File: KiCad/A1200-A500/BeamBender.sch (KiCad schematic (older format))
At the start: 30 parts, among them J1 4-1734742-0, J2 HDMI_A_1.4, J3 STX-3501-3N, J4 Phoenix_Contact, U1 LM1117-3.3, U3 ADV7513BSWZ, X1 Abracon ASE-27.000MHZ-L-R-T

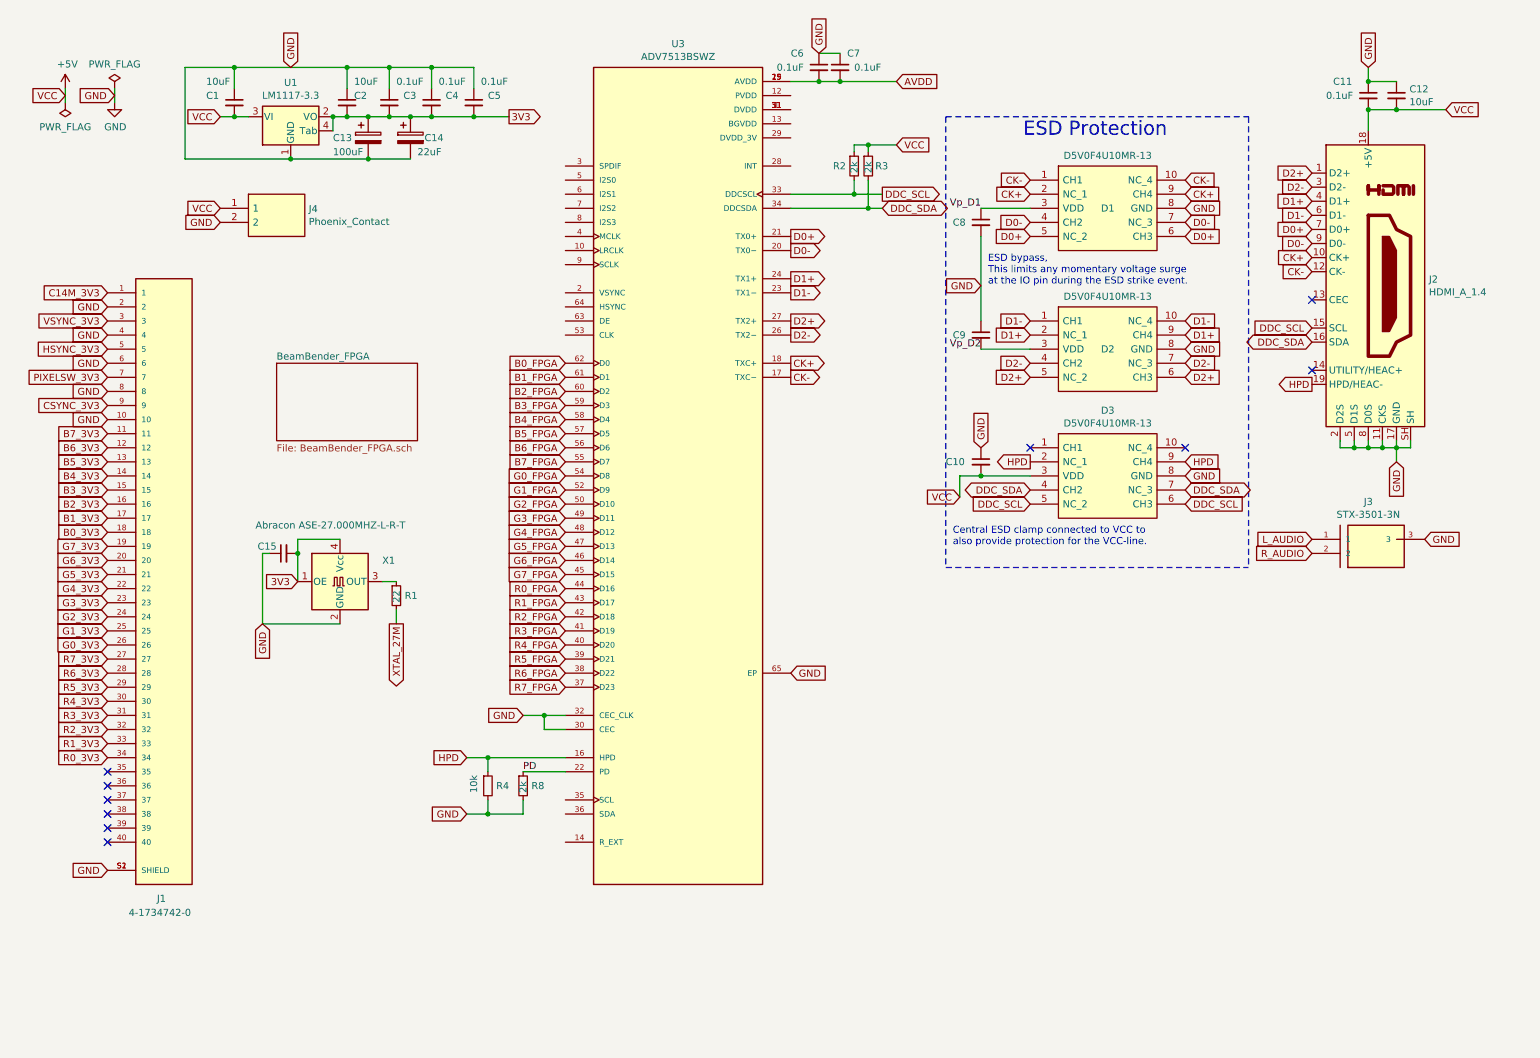
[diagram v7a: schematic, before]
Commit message: Changed to four layer stackup, added some caps and done some more routing
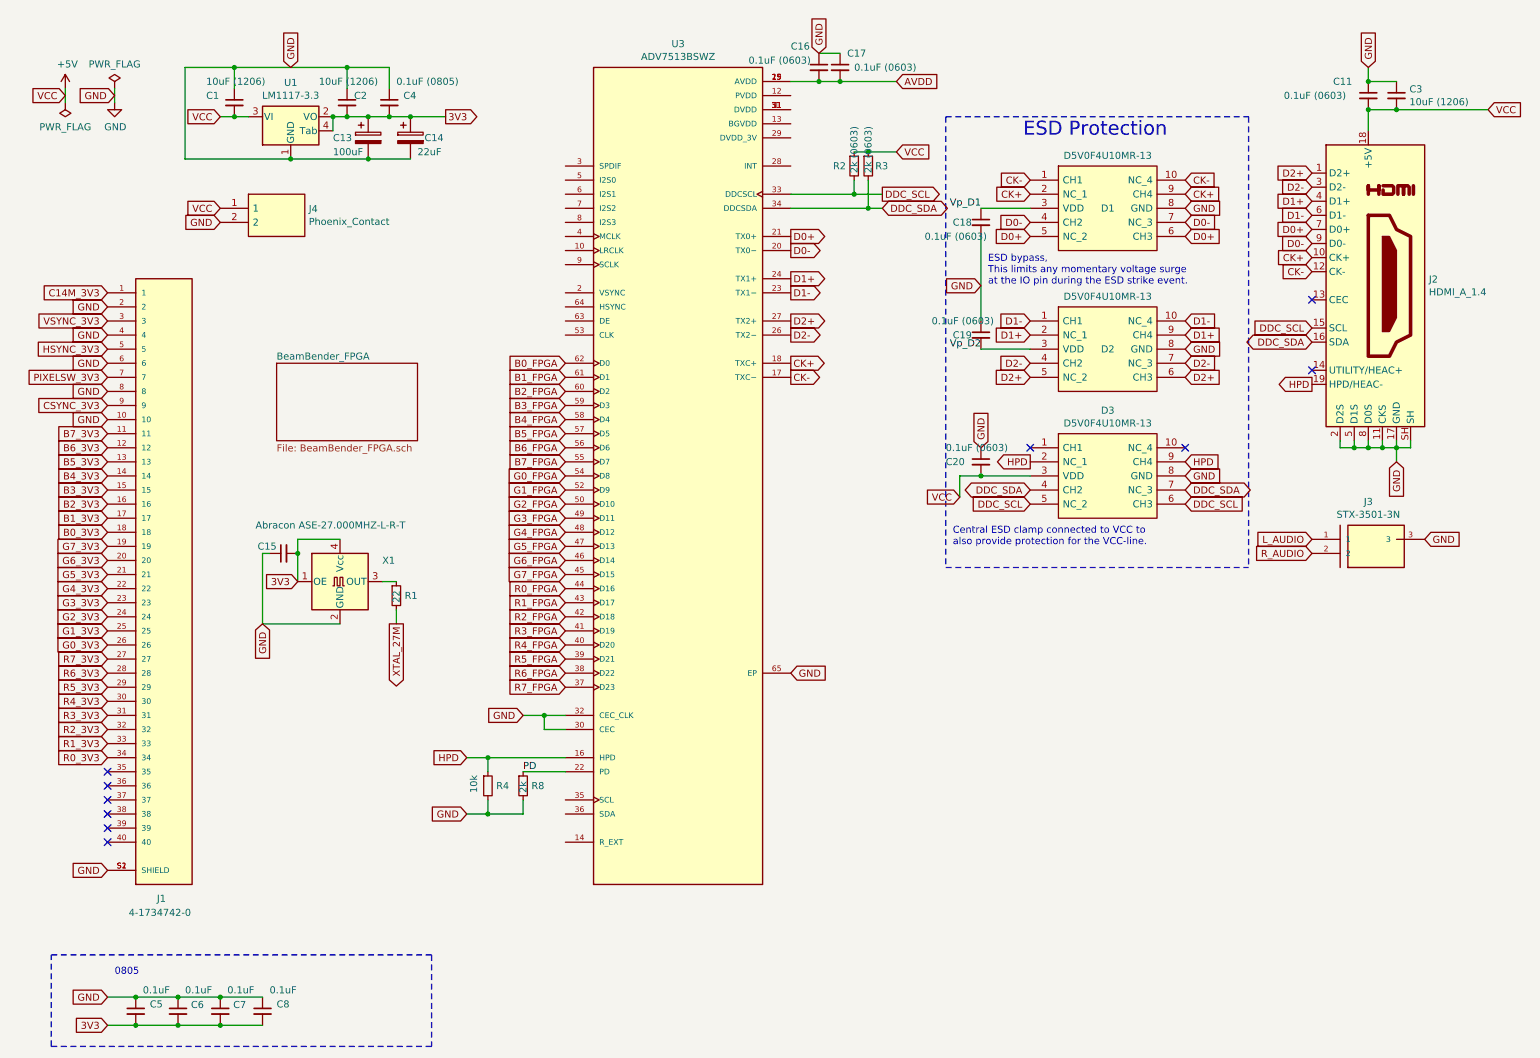
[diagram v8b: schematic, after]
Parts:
- added C6, C7: 0.1uF, Capacitor_SMD:C_0805_2012Metric_Pad1.18x1.45mm_HandSolder, symbol Device:C_Small
- C1, C2: value 10uF -> 10uF (1206)
- C11: value 0.1uF -> 0.1uF (0603)
- C16: renamed from C6; value 0.1uF -> 0.1uF (0603)
- C17: renamed from C7; value 0.1uF -> 0.1uF (0603)
- C18: renamed from C8; value 0.1uF -> 0.1uF (0603)
- C19: renamed from C9; value 0.1uF -> 0.1uF (0603)
- C20: renamed from C10; value 0.1uF -> 0.1uF (0603)
- C3: renamed from C12; value 10uF -> 10uF (1206)
- C4: renamed from C3; value 0.1uF -> 0.1uF (0805)
- R2, R3: value 2k -> 2k (0603)
- renumbered C4 to C5, C5 to C8
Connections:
- net 3V3: now also C6.2, C7.2
- net GND: now also C6.1, C7.1
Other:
- note added: "0805"
- moved on the sheet: C5, C8
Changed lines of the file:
@@
 Text GLabel 2450 800  1    50   Input ~ 0
 GND
-Text GLabel 4000 1150 2    50   Output ~ 0
+Text GLabel 3550 1150 2    50   Output ~ 0
 3V3
 $Comp
@@
 P 2050 1050
 F 0 "C1" H 1850 1100 50  0000 L CNN
-F 1 "10uF" H 1850 1200 50  0000 L CNN
+F 1 "10uF (1206)" H 1850 1200 50  0000 L CNN
 F 2 "Capacitor_SMD:C_1206_3216Metric_Pad1.42x1.75mm_HandSolder" H 2050 1050 50  0001 C CNN
 F 3 "~" H 2050 1050 50  0001 C CNN
@@
 $EndComp
 $Comp
-L Device:C_Small C3
+L Device:C_Small C4
 U 1 1 62475F7C
 P 3150 1050
-F 0 "C3" H 3250 1100 50  0000 L CNN
-F 1 "0.1uF" H 3200 1200 50  0000 L CNN
+F 0 "C4" H 3250 1100 50  0000 L CNN
+F 1 "0.1uF (0805)" H 3200 1200 50  0000 L CNN
 F 2 "Capacitor_SMD:C_0805_2012Metric_Pad1.15x1.40mm_HandSolder" H 3150 1050 50  0001 C CNN
 F 3 "~" H 3150 1050 50  0001 C CNN
@@
 	3150 950  3150 800
 $Comp
-L Device:C_Small C4
+L Device:C_Small C5
 U 1 1 624DDB45
-P 3450 1050
-F 0 "C4" H 3550 1100 50  0000 L CNN
-F 1 "0.1uF" H 3500 1200 50  0000 L CNN
-F 2 "Capacitor_SMD:C_0805_2012Metric_Pad1.15x1.40mm_HandSolder" H 3450 1050 50  0001 C CNN
-F 3 "~" H 3450 1050 50  0001 C CNN
-	1    3450 1050
-	1    0    0    -1
-$EndComp
-$Comp
-L Device:C_Small C5
+P 1350 7500
+F 0 "C5" H 1450 7550 50  0000 L CNN
+F 1 "0.1uF" H 1400 7650 50  0000 L CNN
+F 2 "Capacitor_SMD:C_0805_2012Metric_Pad1.15x1.40mm_HandSolder" H 1350 7500 50  0001 C CNN
+F 3 "~" H 1350 7500 50  0001 C CNN
+	1    1350 7500
+	1    0    0    -1
+$EndComp
+$Comp
+L Device:C_Small C8
 U 1 1 624DE9B4
-P 3750 1050
-F 0 "C5" H 3850 1100 50  0000 L CNN
-F 1 "0.1uF" H 3800 1200 50  0000 L CNN
-F 2 "Capacitor_SMD:C_0805_2012Metric_Pad1.15x1.40mm_HandSolder" H 3750 1050 50  0001 C CNN
-F 3 "~" H 3750 1050 50  0001 C CNN
-	1    3750 1050
+P 2250 7500
+F 0 "C8" H 2350 7550 50  0000 L CNN
+F 1 "0.1uF" H 2300 7650 50  0000 L CNN
+F 2 "Capacitor_SMD:C_0805_2012Metric_Pad1.15x1.40mm_HandSolder" H 2250 7500 50  0001 C CNN
+F 3 "~" H 2250 7500 50  0001 C CNN
+	1    2250 7500
 	1    0    0    -1
 $EndComp
 Wire Wire Line
 	3150 1150 3300 1150
-Connection ~ 3450 1150
-Wire Wire Line
-	3450 1150 3750 1150
-Wire Wire Line
-	3450 950  3450 800
-Wire Wire Line
-	3450 800  3150 800
-Wire Wire Line
-	3750 950  3750 800
-Wire Wire Line
-	3750 800  3450 800
-Connection ~ 3450 800
-Wire Wire Line
-	3750 1150 4000 1150
-Connection ~ 3750 1150
 Text GLabel 1150 2500 0    50   Input ~ 0
 GND
@@
 P 2850 1050
 F 0 "C2" H 2900 1100 50  0000 L CNN
-F 1 "10uF" H 2900 1200 50  0000 L CNN
+F 1 "10uF (1206)" H 2650 1200 50  0000 L CNN
 F 2 "Capacitor_SMD:C_1206_3216Metric_Pad1.42x1.75mm_HandSolder" H 2850 1050 50  0001 C CNN
 F 3 "~" H 2850 1050 50  0001 C CNN
@@
 Wire Wire Line
 	2850 1150 3000 1150
-Connection ~ 3150 800
 Wire Wire Line
 	2850 950  2850 800
@@
 	1    0    0    -1
 $EndComp
-Text GLabel 10650 1100 2    50   Input ~ 0
+Text GLabel 10950 1100 2    50   Input ~ 0
 VCC
 Text GLabel 1150 2400 0    50   Input ~ 0
@@
 GND
 $Comp
-L Device:R_Small R3
-U 1 1 6532BC2D
-P 6550 1500
-F 0 "R3" H 6600 1500 50  0000 L CNN
-F 1 "2k" V 6550 1450 50  0000 L CNN
-F 2 "Resistor_SMD:R_0603_1608Metric_Pad0.98x0.95mm_HandSolder" H 6550 1500 50  0001 C CNN
-F 3 "~" H 6550 1500 50  0001 C CNN
-	1    6550 1500
-	1    0    0    -1
-$EndComp
-$Comp
 L Device:R_Small R2
 U 1 1 6532D8B1
 P 6450 1500
 F 0 "R2" H 6300 1500 50  0000 L CNN
-F 1 "2k" V 6450 1450 50  0000 L CNN
+F 1 "2k  (0603)" V 6450 1450 50  0000 L CNN
 F 2 "Resistor_SMD:R_0603_1608Metric_Pad0.98x0.95mm_HandSolder" H 6450 1500 50  0001 C CNN
 F 3 "~" H 6450 1500 50  0001 C CNN
@@
 	1    0    0    -1
 $EndComp
-Text GLabel 6750 1350 2    50   Input ~ 0
+Text GLabel 6750 1400 2    50   Input ~ 0
 VCC
 Wire Wire Line
@@
 Wire Wire Line
 	6550 1800 6650 1800
-Wire Wire Line
-	6550 1400 6550 1350
-Wire Wire Line
-	6550 1350 6750 1350
-Wire Wire Line
-	6450 1400 6450 1350
-Wire Wire Line
-	6450 1350 6550 1350
-Connection ~ 6550 1350
 Text GLabel 9700 2650 0    50   Input ~ 0
 DDC_SCL
@@
 	6000 900  6200 900
 $Comp
-L Device:C_Small C6
+L Device:C_Small C16
 U 1 1 653C1DFE
 P 6200 800
-F 0 "C6" H 6000 900 50  0000 L CNN
-F 1 "0.1uF" H 5900 800 50  0000 L CNN
+F 0 "C16" H 6000 950 50  0000 L CNN
+F 1 "0.1uF (0603)" H 5700 850 50  0000 L CNN
 F 2 "Capacitor_SMD:C_0603_1608Metric_Pad1.08x0.95mm_HandSolder" H 6200 800 50  0001 C CNN
 F 3 "~" H 6200 800 50  0001 C CNN
@@
 	6200 900  6350 900
 $Comp
-L Device:C_Small C7
+L Device:C_Small C17
 U 1 1 653F698E
 P 6350 800
-F 0 "C7" H 6400 900 50  0000 L CNN
-F 1 "0.1uF" H 6450 800 50  0000 L CNN
+F 0 "C17" H 6400 900 50  0000 L CNN
+F 1 "0.1uF (0603)" H 6450 800 50  0000 L CNN
 F 2 "Capacitor_SMD:C_0603_1608Metric_Pad1.08x0.95mm_HandSolder" H 6350 800 50  0001 C CNN
 F 3 "~" H 6350 800 50  0001 C CNN
@@
 	7700 2800 7350 2800
 $Comp
-L Device:C_Small C9
+L Device:C_Small C19
 U 1 1 65476445
 P 7350 2700
-F 0 "C9" H 7150 2700 50  0000 L CNN
-F 1 "0.1uF" H 7442 2655 50  0001 L CNN
+F 0 "C19" H 7150 2700 50  0000 L CNN
+F 1 "0.1uF (0603)" H 7000 2800 50  0000 L CNN
 F 2 "Capacitor_SMD:C_0603_1608Metric_Pad1.08x0.95mm_HandSolder" H 7350 2700 50  0001 C CNN
 F 3 "~" H 7350 2700 50  0001 C CNN
@@
 $EndComp
 $Comp
-L Device:C_Small C8
+L Device:C_Small C18
 U 1 1 6547758E
 P 7350 1900
-F 0 "C8" H 7150 1900 50  0000 L CNN
-F 1 "0.1uF" H 7442 1855 50  0001 L CNN
+F 0 "C18" H 7150 1900 50  0000 L CNN
+F 1 "0.1uF (0603)" H 6950 1800 50  0000 L CNN
 F 2 "Capacitor_SMD:C_0603_1608Metric_Pad1.08x0.95mm_HandSolder" H 7350 1900 50  0001 C CNN
 F 3 "~" H 7350 1900 50  0001 C CNN
@@
 	7700 1800 7350 1800
 $Comp
-L Device:C_Small C10
+L Device:C_Small C20
 U 1 1 6548D3D3
 P 7350 3600
-F 0 "C10" H 7100 3600 50  0000 L CNN
-F 1 "0.1uF" H 7442 3555 50  0001 L CNN
+F 0 "C20" H 7100 3600 50  0000 L CNN
+F 1 "0.1uF (0603)" H 7100 3700 50  0000 L CNN
 F 2 "Capacitor_SMD:C_0603_1608Metric_Pad1.08x0.95mm_HandSolder" H 7350 3600 50  0001 C CNN
 F 3 "~" H 7350 3600 50  0001 C CNN
@@
 P 10100 1000
 F 0 "C11" H 9850 1100 50  0000 L CNN
-F 1 "0.1uF" H 9800 1000 50  0000 L CNN
+F 1 "0.1uF (0603)" H 9500 1000 50  0000 L CNN
 F 2 "Capacitor_SMD:C_0603_1608Metric_Pad1.08x0.95mm_HandSolder" H 10100 1000 50  0001 C CNN
 F 3 "~" H 10100 1000 50  0001 C CNN
@@
 	7350 2000 7350 2600
 $Comp
-L Device:C_Small C12
+L Device:C_Small C3
 U 1 1 654D36E6
 P 10300 1000
-F 0 "C12" H 10392 1046 50  0000 L CNN
-F 1 "10uF" H 10392 955 50  0000 L CNN
+F 0 "C3" H 10392 1046 50  0000 L CNN
+F 1 "10uF (1206)" H 10392 955 50  0000 L CNN
 F 2 "Capacitor_SMD:C_1206_3216Metric_Pad1.33x1.80mm_HandSolder" H 10300 1000 50  0001 C CNN
 F 3 "~" H 10300 1000 50  0001 C CNN
@@
 	10100 1100 10300 1100
 Connection ~ 10300 1100
-Wire Wire Line
-	10300 1100 10650 1100
 $Comp
 L BeamBender:Phoenix_Contact J4
@@
 	1    0    0    -1
 $EndComp
-Connection ~ 3300 1150
-Wire Wire Line
-	3300 1150 3450 1150
 Wire Wire Line
 	3000 1450 3300 1450
@@
 Wire Wire Line
 	3200 4650 3200 4750
+Text GLabel 1150 7600 0    50   Input ~ 0
+3V3
+Wire Wire Line
+	1150 7600 1350 7600
+Connection ~ 1350 7600
+Wire Wire Line
+	1350 7600 1650 7600
+Text GLabel 1150 7400 0    50   Input ~ 0
+GND
+Wire Wire Line
+	1150 7400 1350 7400
+Connection ~ 1350 7400
+Wire Wire Line
+	1350 7400 1650 7400
+Wire Wire Line
+	3300 1150 3550 1150
+Connection ~ 3300 1150
+$Comp
+L Device:R_Small R3
+U 1 1 6532BC2D
+P 6550 1500
+F 0 "R3" H 6600 1500 50  0000 L CNN
+F 1 "2k  (0603)" V 6550 1450 50  0000 L CNN
+F 2 "Resistor_SMD:R_0603_1608Metric_Pad0.98x0.95mm_HandSolder" H 6550 1500 50  0001 C CNN
+F 3 "~" H 6550 1500 50  0001 C CNN
+	1    6550 1500
+	1    0    0    -1
+$EndComp
+Wire Wire Line
+	10300 1100 10950 1100
+Wire Wire Line
+	6450 1400 6550 1400
+Connection ~ 6550 1400
+Wire Wire Line
+	6550 1400 6750 1400
+Text Notes 1200 7250 0    50   ~ 0
+0805
+Wire Notes Line
+	750  7100 3450 7100
+Wire Notes Line
+	3450 7100 3450 7750
+Wire Notes Line
+	3450 7750 750  7750
+Wire Notes Line
+	750  7750 750  7100
+Wire Wire Line
+	1650 7400 1950 7400
+Connection ~ 1650 7400
+Wire Wire Line
+	1650 7600 1950 7600
+Connection ~ 1650 7600
+$Comp
+L Device:C_Small C6
+U 1 1 65576E27
+P 1650 7500
+F 0 "C6" H 1742 7546 50  0000 L CNN
+F 1 "0.1uF" H 1700 7650 50  0000 L CNN
+F 2 "Capacitor_SMD:C_0805_2012Metric_Pad1.18x1.45mm_HandSolder" H 1650 7500 50  0001 C CNN
+F 3 "~" H 1650 7500 50  0001 C CNN
+	1    1650 7500
+	1    0    0    -1
+$EndComp
+$Comp
+L Device:C_Small C7
+U 1 1 6558592E
+P 1950 7500
+F 0 "C7" H 2042 7546 50  0000 L CNN
+F 1 "0.1uF" H 2000 7650 50  0000 L CNN
+F 2 "Capacitor_SMD:C_0805_2012Metric_Pad1.18x1.45mm_HandSolder" H 1950 7500 50  0001 C CNN
+F 3 "~" H 1950 7500 50  0001 C CNN
+	1    1950 7500
+	1    0    0    -1
+$EndComp
+Wire Wire Line
+	1950 7400 2250 7400
+Connection ~ 1950 7400
+Wire Wire Line
+	1950 7600 2250 7600
+Connection ~ 1950 7600
 $EndSCHEMATC
